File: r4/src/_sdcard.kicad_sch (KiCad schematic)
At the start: 6 parts, among them J14 Micro_SD_Card_Det_JAE_ST11, U10 ESD7004, U11 ESD7004

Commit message: Update files to Kicad 6 format
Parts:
- ?: renamed from J14; value Micro_SD_Card_Det_JAE_ST11 -> (none); footprint jeffmakes-footprints:microSD_JAE_ST11S008V4H -> (none)
- ?: renamed from R24; value 100k -> (none); footprint Resistor_SMD:R_0603_1608Metric -> (none)
- ?: renamed from C30; value 100nF -> (none); footprint Capacitor_SMD:C_0603_1608Metric -> (none)
- ?: renamed from C29; value 47uF -> (none); footprint Capacitor_SMD:C_0805_2012Metric -> (none)
- ?: renamed from U10; value ESD7004 -> (none); footprint jeffmakes-footprints:USON-10_2.5x1.0mm_P0.5mm -> (none)
- ?: renamed from U11; value ESD7004 -> (none); footprint jeffmakes-footprints:USON-10_2.5x1.0mm_P0.5mm -> (none)

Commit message: Add netclass definitions and assign nets. Define DRC rules to each class. Resize all vias and nets (with a few exceptions for very wide power tracks) to follow the netclass rules. Increase area for GNDA domain. Re-route SIM data bus around edge of GNDA domain
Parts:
- C29: renamed from ?; value (none) -> 47uF; footprint (none) -> Capacitor_SMD:C_0805_2012Metric
- C30: renamed from ?; value (none) -> 100nF; footprint (none) -> Capacitor_SMD:C_0603_1608Metric
- J14: renamed from ?; value (none) -> Micro_SD_Card_Det_JAE_ST11; footprint (none) -> jeffmakes-footprints:microSD_JAE_ST11S008V4H
- R24: renamed from ?; value (none) -> 100k; footprint (none) -> Resistor_SMD:R_0603_1608Metric
- U10, U11: renamed from ?; value (none) -> ESD7004; footprint (none) -> Package_SON:USON-10_2.5x1.0mm_P0.5mm

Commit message: Set volage ratings on some caps, change some cap footprints to remove a couple of BOM lines
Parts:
- C29: Voltage (none) -> 6.3V
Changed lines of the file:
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@@
+      (effects (font (size 1.27 1.27)) hide)
+    )
+    (property "Voltage" "6.3V" (at 162.56 74.93 0)
       (effects (font (size 1.27 1.27)) hide)
     )

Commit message: Shrink some resistors to 0402
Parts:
- R24: footprint Resistor_SMD:R_0603_1608Metric -> Resistor_SMD:R_0402_1005Metric
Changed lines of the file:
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@@
       (effects (font (size 1.27 1.27)) (justify right))
     )
-    (property "Footprint" "Resistor_SMD:R_0603_1608Metric" (at 144.78 83.82 0)
+    (property "Footprint" "Resistor_SMD:R_0402_1005Metric" (at 144.78 83.82 0)
       (effects (font (size 1.27 1.27)) hide)
     )
@@
       (project "bugg-main-r4"
         (path "/e3eb514f-6ce4-4abe-ba20-f82f0015628f/498d2354-7ecc-4881-a4b8-afc4730b4589"
-          (reference "R24") (unit 1) (value "100k") (footprint "Resistor_SMD:R_0603_1608Metric")
+          (reference "R24") (unit 1) (value "100k") (footprint "Resistor_SMD:R_0402_1005Metric")
         )
       )

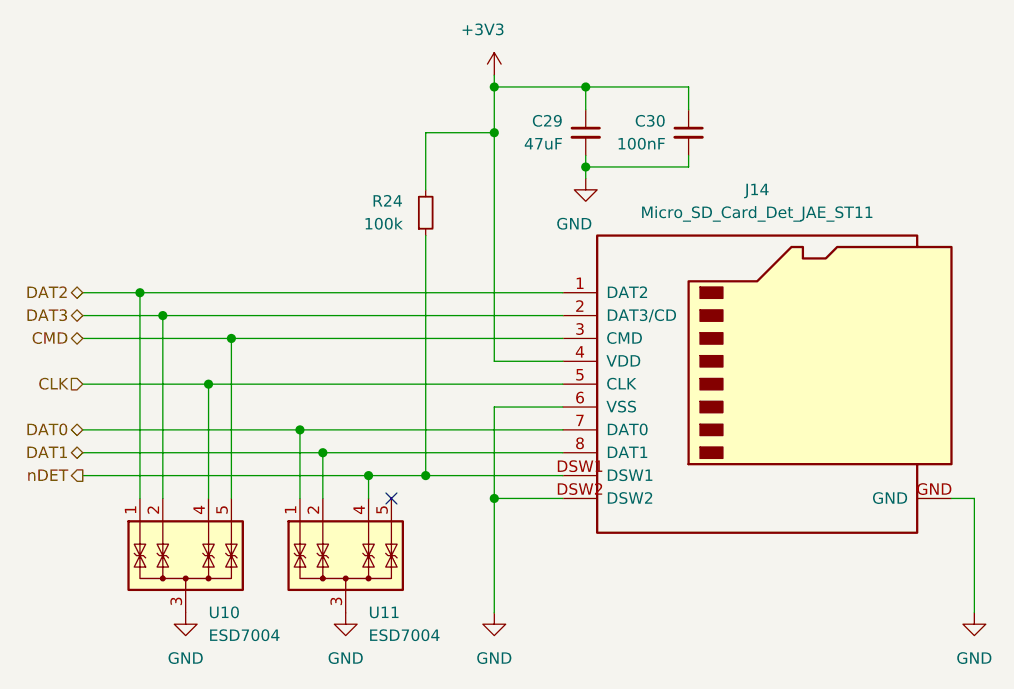
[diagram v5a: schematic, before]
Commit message: Update TVS packs with pass-through routing
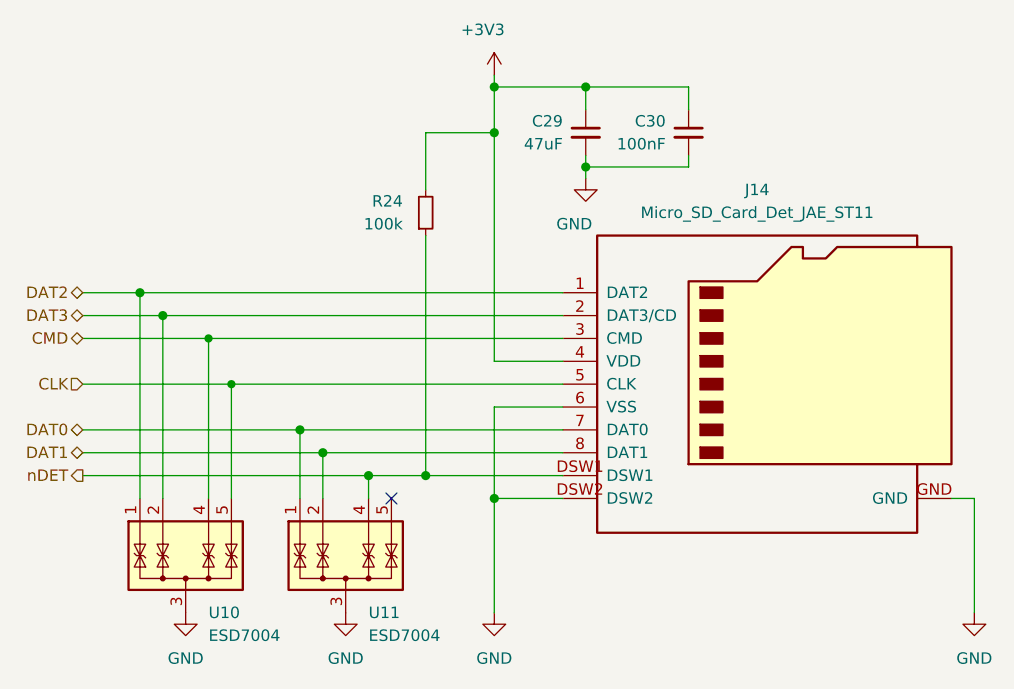
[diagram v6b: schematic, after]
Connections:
- net CLK: now also U10.5 (IO4), U10.6; no longer U10.4 (IO3)
- net CMD: now also U10.4 (IO3), U10.7; no longer U10.5 (IO4)
- net DAT0: now also U11.10
- net DAT1: now also U11.9
- net DAT2: now also U10.10
- net DAT3: now also U10.9
- net GND: now also U10.8, U11.8
- net nDET: now also U11.7
- net at U11.5 (IO4): now also U11.6
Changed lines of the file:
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@@
   (junction (at 162.56 69.85) (diameter 1.016) (color 0 0 0 0)
   )
+  (junction (at 123.19 102.87) (diameter 0) (color 0 0 0 0)
+  )
   (junction (at 152.4 115.57) (diameter 1.016) (color 0 0 0 0)
   )
   (junction (at 162.56 78.74) (diameter 1.016) (color 0 0 0 0)
   )
+  (junction (at 120.65 97.79) (diameter 0) (color 0 0 0 0)
+  )
   (junction (at 130.81 107.95) (diameter 1.016) (color 0 0 0 0)
   )
@@
   (junction (at 138.43 113.03) (diameter 1.016) (color 0 0 0 0)
   )
-  (junction (at 120.65 102.87) (diameter 1.016) (color 0 0 0 0)
-  )
   (junction (at 152.4 74.93) (diameter 1.016) (color 0 0 0 0)
   )
   (junction (at 133.35 110.49) (diameter 1.016) (color 0 0 0 0)
-  )
-  (junction (at 123.19 97.79) (diameter 1.016) (color 0 0 0 0)
   )
   (no_connect (at 140.97 115.57))
@@
     (stroke (width 0) (type solid))
   )
+  (wire (pts (xy 123.19 102.87) (xy 123.19 115.57))
+    (stroke (width 0) (type default))
+  )
   (wire (pts (xy 138.43 113.03) (xy 138.43 115.57))
     (stroke (width 0) (type solid))
   )
+  (wire (pts (xy 123.19 102.87) (xy 160.02 102.87))
+    (stroke (width 0) (type solid))
+  )
   (wire (pts (xy 113.03 92.71) (xy 113.03 115.57))
     (stroke (width 0) (type solid))
@@
     (stroke (width 0) (type solid))
   )
-  (wire (pts (xy 106.68 102.87) (xy 120.65 102.87))
-    (stroke (width 0) (type solid))
-  )
-  (wire (pts (xy 120.65 102.87) (xy 160.02 102.87))
+  (wire (pts (xy 106.68 102.87) (xy 123.19 102.87))
     (stroke (width 0) (type solid))
   )
@@
     (stroke (width 0) (type solid))
   )
+  (wire (pts (xy 120.65 97.79) (xy 120.65 115.57))
+    (stroke (width 0) (type default))
+  )
   (wire (pts (xy 133.35 110.49) (xy 133.35 115.57))
     (stroke (width 0) (type solid))
@@
     (stroke (width 0) (type solid))
   )
-  (wire (pts (xy 106.68 97.79) (xy 123.19 97.79))
-    (stroke (width 0) (type solid))
-  )
-  (wire (pts (xy 123.19 97.79) (xy 160.02 97.79))
+  (wire (pts (xy 106.68 97.79) (xy 120.65 97.79))
+    (stroke (width 0) (type solid))
+  )
+  (wire (pts (xy 120.65 97.79) (xy 160.02 97.79))
     (stroke (width 0) (type solid))
   )
@@
   )
   (wire (pts (xy 152.4 100.33) (xy 160.02 100.33))
-    (stroke (width 0) (type solid))
-  )
-  (wire (pts (xy 123.19 97.79) (xy 123.19 115.57))
-    (stroke (width 0) (type solid))
-  )
-  (wire (pts (xy 120.65 102.87) (xy 120.65 115.57))
     (stroke (width 0) (type solid))
   )
@@
     (pin "3")
     (pin "1")
+    (pin "10")
     (pin "2")
     (pin "4")
     (pin "5")
+    (pin "6")
+    (pin "7")
+    (pin "8")
+    (pin "9")
     (instances
       (project "bugg-main-r4"
@@
     )
   )
-  (symbol (lib_id "j_Power_Protection:ESD7004") (at 135.89 123.19 0) (unit 1)
+  (symbol (lib_name "ESD7004_1") (lib_id "j_Power_Protection:ESD7004") (at 135.89 123.19 0) (unit 1)
     (in_bom yes) (on_board yes) (dnp no)
     (property "Reference" "U11" (at 138.43 128.27 0)
@@
     (pin "3")
     (pin "1")
+    (pin "10")
     (pin "2")
     (pin "4")
     (pin "5")
-    (instances
-      (project "bugg-main-r4"
+    (pin "6")
+    (pin "7")
+    (pin "8")
+    (pin "9")
+    (instances
+      (project "bugg-main-r4"
